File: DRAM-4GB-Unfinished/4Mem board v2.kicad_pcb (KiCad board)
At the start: 6 copper layers, 150.4 x 75.2 mm, 75 parts, among them P1 CONN_1, P11 CONN_2X2, P2 CONN_1, P3 CONN_1, P4 CONN_1, P8 CONN_20X2, P9 CONN_20X2, Q1 ^^NPN-BC817-SOT323, SW1 PROG_B, U1 XC6SLX45-2FGG484C, U2 DDR3_DIMM_240PIN, U3 XCF08P-VO48/TSOP48, U4 LM1117MP-1.8, U5 AZ1084, U6 NCP565, U7 LT1764EQ-1.5, U8 RT9026_MSOP-10

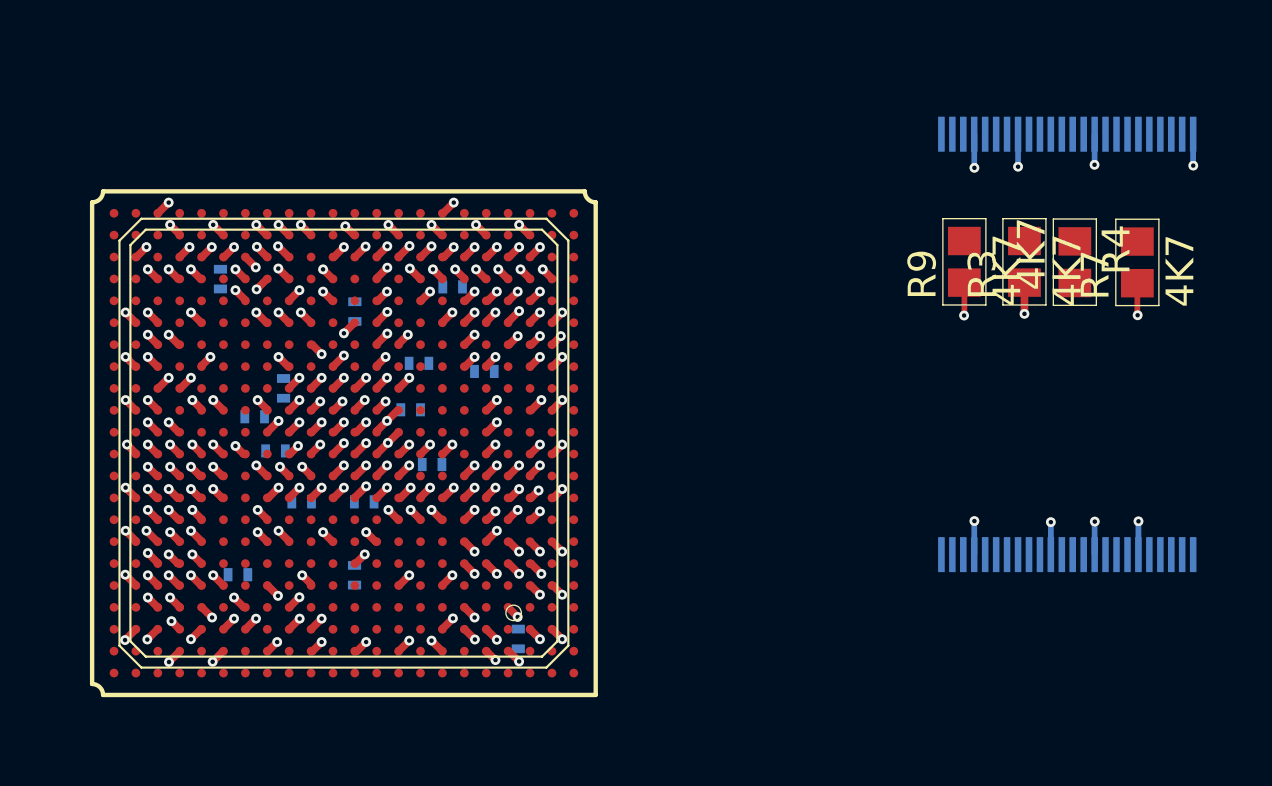
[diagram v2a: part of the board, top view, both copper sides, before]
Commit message: DRAM-4GB-Unfinished: more power routing
Source: S100 4GB DRAM BOARD/4Mem board v2/backups/31-05-2015 1132 (newest file is 2015-05-24; schematic re-saved unchanged)
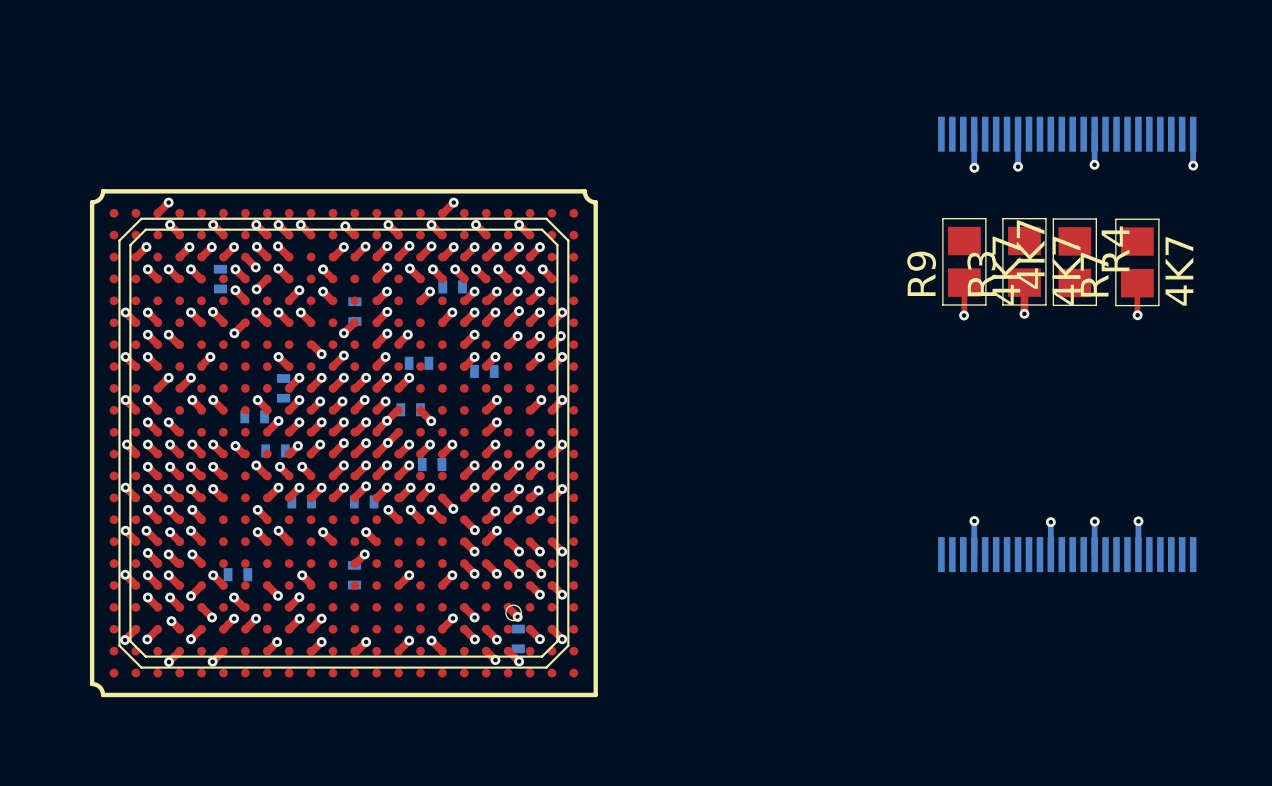
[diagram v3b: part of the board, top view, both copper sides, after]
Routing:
- net GND: track 38.6 -> 186.3 mm
- net /V1.5temp: track 13.1 -> 131.0 mm
- net /V3.3temp: track 22.6 -> 130.5 mm, vias 34 -> 35
- net /V3.3temp2: track 11.9 -> 54.7 mm
- net /V1.8: track 13.4 -> 40.3 mm
- net /V1.2temp: track 13.3 -> 39.4 mm
- net /IO_028: track 0.00 -> 0.71 mm, vias 0 -> 1
- net /IO_029: track 0.00 -> 0.70 mm, vias 0 -> 1

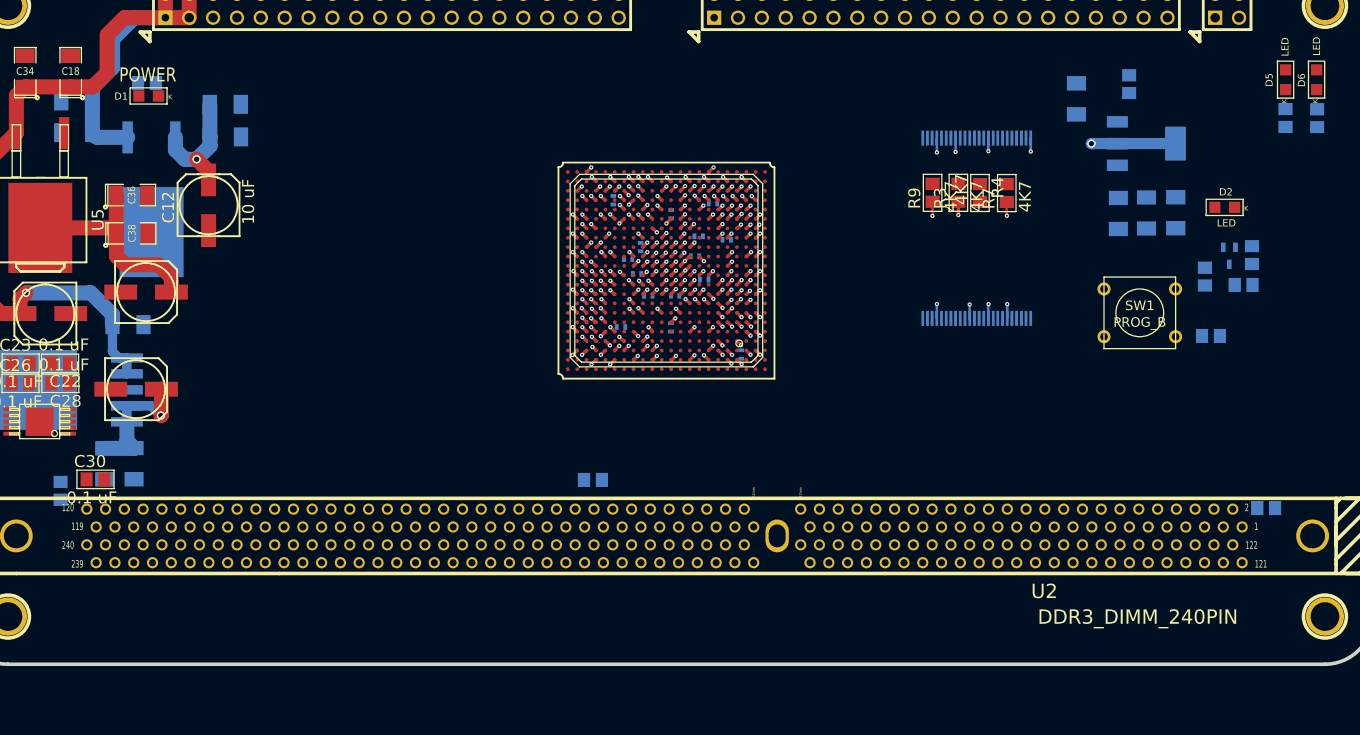
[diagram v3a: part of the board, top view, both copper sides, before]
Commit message: DRAM-4GB-Unfinished: add PIC18F2520, XCF08P config flash and 2.5 V clock; last PCB edits; DigiKey parts list
Source: S100 4GB DRAM BOARD/4Mem board v2/(top level) (working folder; .dsn/.ses/.bak, BMP screenshots, datasheets and saved web pages left out)
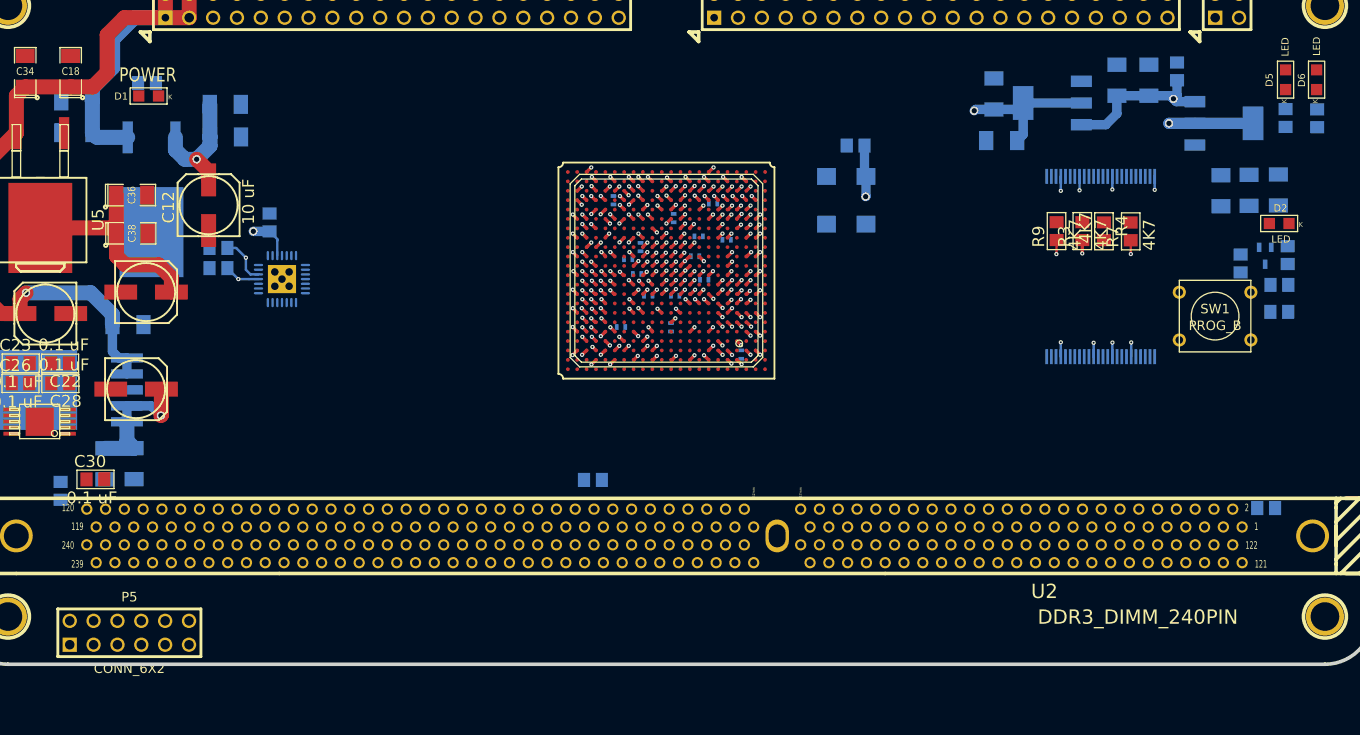
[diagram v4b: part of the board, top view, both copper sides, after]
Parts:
- added C44: 10 uF, SM1206_Opendous, B.Cu at (231.1, 90.5)
- added C45: 0.1 uF, ^^SMD_Resistor-0805, B.Cu at (137.5, 105.6)
- added C46: 10 uF, SM1206_Opendous, B.Cu at (215.4, 96.9)
- added C47: 10 uF, SM1206_Opendous, B.Cu at (214.6, 91.9)
- added C48: 10 uF, ^^SMD_Resistor-0805, B.Cu at (199.8, 97.4)
- added P5: CONN_6X2, PIN_ARRAY_6x2, F.Cu at (122.5, 149.3)
- added R12: 10K, ^^SMD_Resistor-0805, B.Cu at (132.0, 110.5)
- added R13: 10K, ^^SMD_Resistor-0805, B.Cu at (132.0, 108.3)
- added U10: LM1117MP-2.5, ^^SOT223v1, B.Cu at (220.8, 92.9)
- added U12: PIC18F2520-28QFN, ^^QFN28, B.Cu at (138.8, 111.6)
- added U9: FPGA_CLK_0, ^^SMD_HCMOS_TTL_Clock_Oscillator, B.Cu at (196.7, 105.8)
- moved R3 13.8 mm to (224.0, 106.5)
- moved R7 13.8 mm to (229.1, 106.6)
- moved R9 13.8 mm to (221.2, 106.5)
- moved U3 13.8 mm to (225.9, 110.3)
- moved R4 13.8 mm to (226.3, 106.6)
- moved C19 11.2 mm to (238.7, 102.2)
- moved C11 11.2 mm to (244.9, 102.2)
- moved C15 11.2 mm to (241.7, 102.2)
- moved U4 8.53 mm to (239.1, 95.1)
- moved SW1 8.02 mm to (238.1, 115.6)
- moved R10 7.70 mm to (244.9, 115.1)
- moved D2 6.05 mm to (244.9, 105.7)
- moved C3 5.27 mm to (234.1, 89.5)
- moved C8 4.74 mm to (227.7, 90.5)
- moved R8 4.05 mm to (240.8, 110.0)
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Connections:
- U1 pad M3: (no net) -> /FPGA_CLK_0
- U1 pad R15: (no net) -> /PIC_IO6
- U1 pad R16: (no net) -> /PIC_IO5
- U1 pad V11: (no net) -> /PIC_IO2
- U1 pad V18: (no net) -> /PIC_IO4
- U1 pad V19: (no net) -> /PIC_IO3
- U1 pad W11: (no net) -> /PIC_IO1
- U2 pad 118: (no net) -> /DDR3_SCL
- U2 pad 168: (no net) -> /DONE_LED_SIGNAL
- U2 pad 238: (no net) -> /DDR3_SDA
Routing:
- net /V2.5: track 0.00 -> 26.7 mm, vias 0 -> 2
- net /+8Vitemp: track 0.00 -> 16.9 mm, vias 0 -> 1
- net /V1.5temp: track 131.0 -> 138.3 mm, vias 20 -> 21
- net /V3.3temp: track 130.5 -> 124.6 mm
- net /DDR3_SDA: track 0.00 -> 5.24 mm, vias 0 -> 1
- net /V3.3: track 23.2 -> 27.8 mm, vias 0 -> 1
- net /DDR3_SCL: track 0.00 -> 3.79 mm, vias 0 -> 1
- net /PIC_IO2: track 0.00 -> 0.72 mm, vias 0 -> 1
- net /PIC_IO4: track 0.00 -> 0.71 mm, vias 0 -> 1
- net /PIC_IO6: track 0.00 -> 0.71 mm, vias 0 -> 1
- net /PIC_IO5: track 0.00 -> 0.70 mm, vias 0 -> 1
- net /PIC_IO3: track 0.00 -> 0.70 mm, vias 0 -> 1
- net /PIC_IO1: track 0.00 -> 0.70 mm, vias 0 -> 1
